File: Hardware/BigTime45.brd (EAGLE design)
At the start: 24.9 x 24.9 mm, 18 parts, among them J1 AVR_SPI_PRG_6TESTPOINTS-SM, U2 ATMEGA328P_TQFP, Y1 32.768kHz

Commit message: tweak
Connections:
- net A: now also J1.3
- net E: no longer J1.3
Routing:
- net E: track 29.6 -> 21.6 mm
- net D: track 15.0 -> 18.6 mm
- net A: track 9.52 -> 12.6 mm
- net F: track 14.7 -> 17.7 mm
- net B: track 24.0 -> 26.4 mm
- net GND: track 44.2 -> 43.4 mm
- net N$6: track 9.03 -> 9.71 mm
- net DIG2: track 32.1 -> 31.5 mm
- net G: track 10.6 -> 11.1 mm

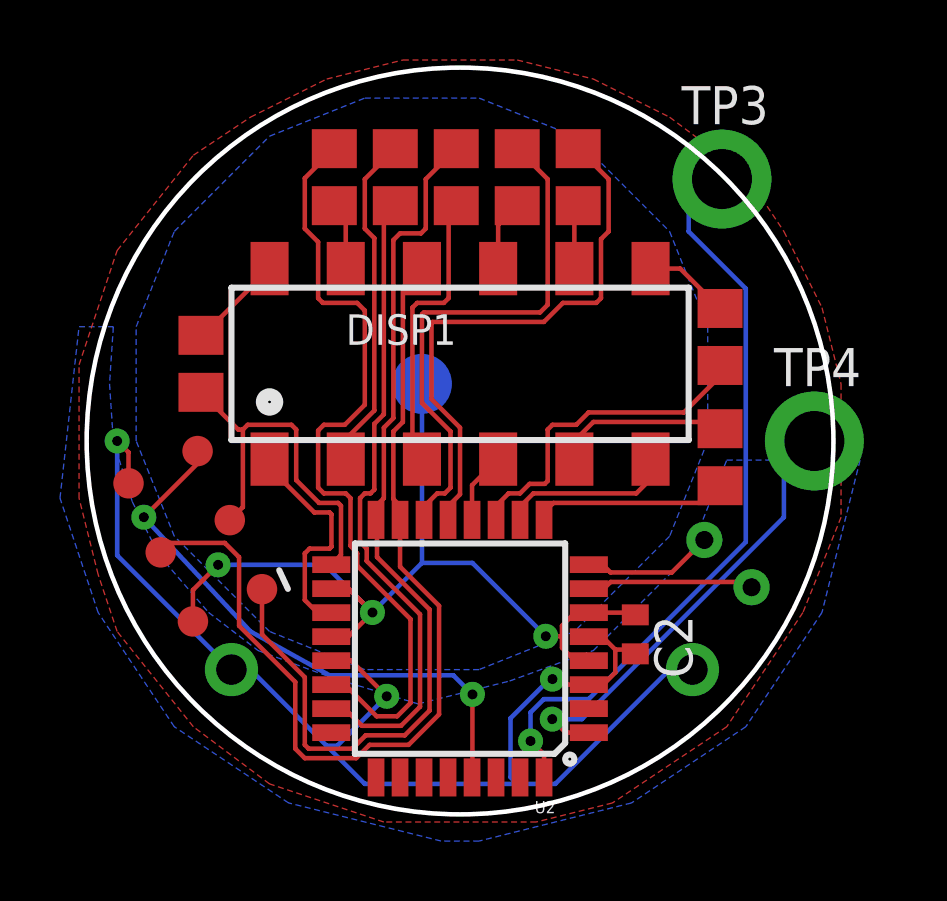
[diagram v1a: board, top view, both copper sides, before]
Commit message: change to 0805 capacitor
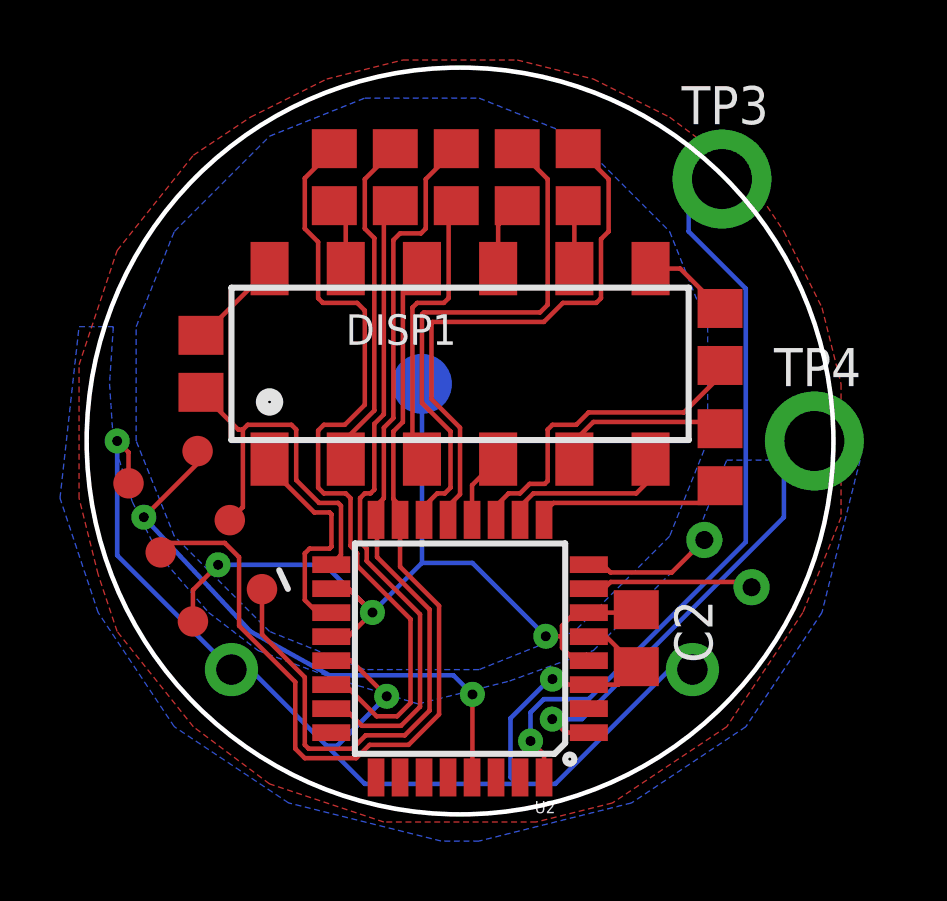
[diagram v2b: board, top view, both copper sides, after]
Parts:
- C2: device resistor:C0402 -> resistor:C0805
- moved C2 0.13 mm to (20.5, 9.94)
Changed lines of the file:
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@@
 </autorouter>
 <elements>
-<element name="C2" library="resistor" package="C0402" value="100nF" x="20.447" y="10.06475" rot="R270"/>
+<element name="C2" library="resistor" package="C0805" value="100nF" x="20.47875" y="9.93775" rot="R270"/>
 <element name="Y1" library="BigTime" package="TC26H" value="32.768kHz" x="22.63775" y="11.52525" smashed="yes" rot="MR225">
 <attribute name="NAME" x="20.213071875" y="11.076240625" size="1.27" layer="26" ratio="10" rot="MR315" display="off"/>
@@
 <wire x1="18.00225" y1="9.62025" x2="18.00225" y2="10.00125" width="0.1524" layer="1"/>
 <wire x1="18.00225" y1="10.00125" x2="18.00225" y2="10.3505" width="0.1524" layer="1"/>
-<wire x1="20.447" y1="10.71475" x2="20.432" y2="10.683" width="0.1524" layer="1"/>
-<wire x1="20.432" y1="10.683" x2="20.32" y2="10.795" width="0.1524" layer="1"/>
-<wire x1="18.8976" y1="10.7885" x2="20.37325" y2="10.7885" width="0.1524" layer="1"/>
 <wire x1="13.335" y1="12.446" x2="15.01775" y2="12.446" width="0.1524" layer="16"/>
 <wire x1="15.01775" y1="12.446" x2="17.4625" y2="10.00125" width="0.1524" layer="16"/>
@@
 <wire x1="10.8775" y1="9.9885" x2="10.3124" y2="9.9885" width="0.1524" layer="1"/>
 <via x="6.5405" y="12.3825" extent="1-16" drill="0.3302"/>
-<wire x1="20.447" y1="10.71475" x2="20.37325" y2="10.7885" width="0.1524" layer="1"/>
 <wire x1="5.7009375" y1="10.49625" x2="5.7009375" y2="11.5429375" width="0.1524" layer="1"/>
 <wire x1="5.7009375" y1="11.5429375" x2="6.5405" y2="12.3825" width="0.1524" layer="1"/>
 <wire x1="6.5405" y1="12.3825" x2="10.0965" y2="12.3825" width="0.1524" layer="16"/>
 <wire x1="10.0965" y1="12.3825" x2="11.684" y2="10.795" width="0.1524" layer="16"/>
+<wire x1="20.47875" y1="10.88775" x2="20.3795" y2="10.7885" width="0.1524" layer="1"/>
+<wire x1="20.3795" y1="10.7885" x2="18.8976" y2="10.7885" width="0.1524" layer="1"/>
 </signal>
 <signal name="DIG1">
@@
 <contactref element="TP6" pad="1"/>
 <contactref element="J1" pad="6"/>
-<wire x1="18.8976" y1="8.3885" x2="19.374" y2="8.3885" width="0.1524" layer="1"/>
-<wire x1="19.374" y1="8.3885" x2="19.78025" y2="8.79475" width="0.1524" layer="1"/>
-<wire x1="19.78025" y1="8.79475" x2="19.78025" y2="9.55675" width="0.1524" layer="1"/>
-<wire x1="18.8976" y1="9.9885" x2="19.3485" y2="9.9885" width="0.1524" layer="1"/>
-<wire x1="19.3485" y1="9.9885" x2="19.78025" y2="9.55675" width="0.1524" layer="1"/>
 <via x="17.68475" y="8.5725" extent="1-16" drill="0.3302"/>
 <wire x1="17.78" y1="5.08" x2="21.59" y2="8.89" width="0.1524" layer="16"/>
@@
 <wire x1="10.50925" y1="6.35" x2="10.16" y2="6.35" width="0.1524" layer="16"/>
 <wire x1="10.97275" y1="9.1885" x2="12.16025" y2="8.001" width="0.1524" layer="1"/>
-<wire x1="20.447" y1="9.41475" x2="20.305" y2="9.55675" width="0.1524" layer="1"/>
-<wire x1="20.305" y1="9.55675" x2="19.78025" y2="9.55675" width="0.1524" layer="1"/>
 <wire x1="17.68475" y1="8.5725" x2="17.5895" y2="8.5725" width="0.1524" layer="16"/>
 <wire x1="17.5895" y1="8.5725" x2="16.28775" y2="7.27075" width="0.1524" layer="16"/>
 <wire x1="16.28775" y1="7.27075" x2="16.28775" y2="5.30225" width="0.1524" layer="16"/>
 <wire x1="16.28775" y1="5.30225" x2="16.51" y2="5.08" width="0.1524" layer="16"/>
+<wire x1="20.47875" y1="8.98775" x2="19.478" y2="9.9885" width="0.1524" layer="1"/>
+<wire x1="19.478" y1="9.9885" x2="18.8976" y2="9.9885" width="0.1524" layer="1"/>
+<wire x1="20.47875" y1="8.98775" x2="19.8795" y2="8.3885" width="0.1524" layer="1"/>
+<wire x1="19.8795" y1="8.3885" x2="18.8976" y2="8.3885" width="0.1524" layer="1"/>
 </signal>
 <signal name="28">
